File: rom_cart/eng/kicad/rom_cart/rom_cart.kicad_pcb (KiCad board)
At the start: 2 copper layers, 128.3 x 99.1 mm, 12 parts, among them J1 CONN_A2K6_CART_CARD, J2 CONN_512K_CART_CARD, SW1 SW_DIP_x04, SW2 SW_DIP_x04, U1 SST39SF040-70-4C-NHE, U2 74AHCT1G04

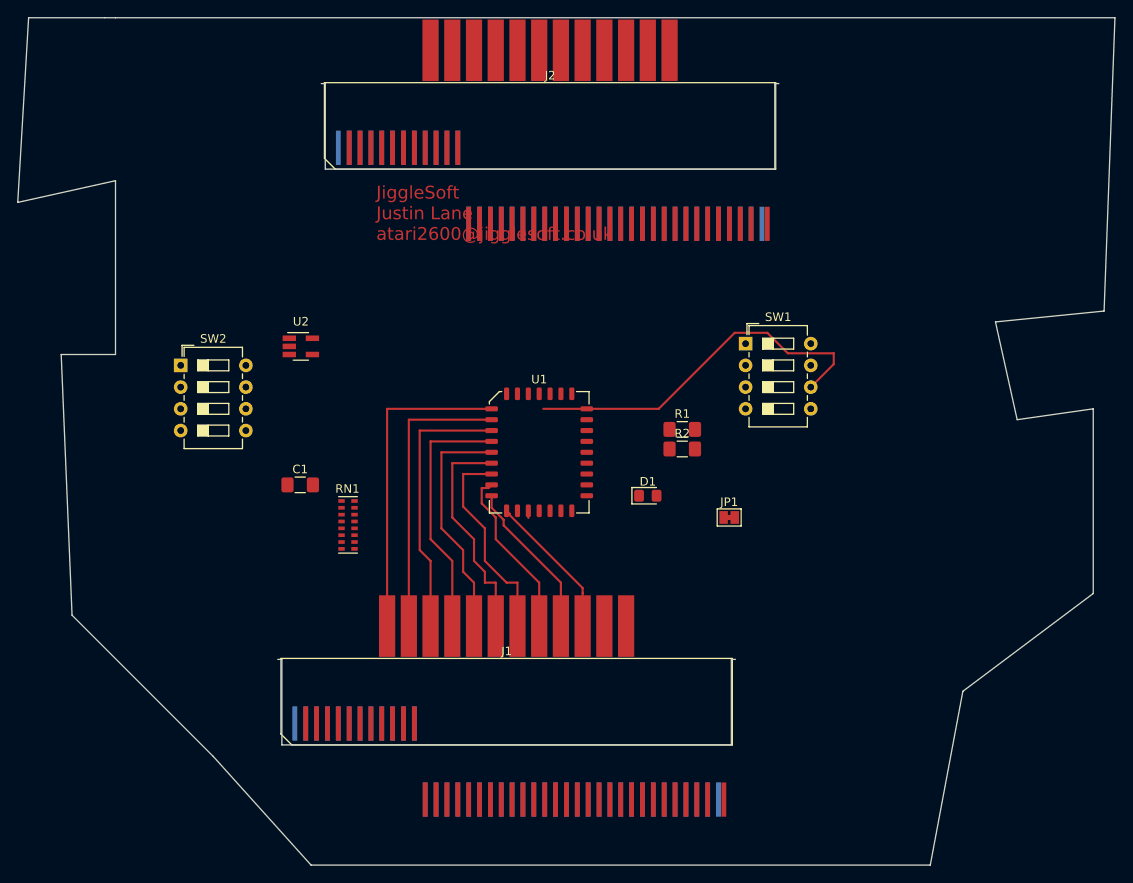
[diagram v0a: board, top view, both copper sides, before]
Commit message: Atari 2600 Budget Flash ROM Cartridge PCB layout Work-In-Progress.
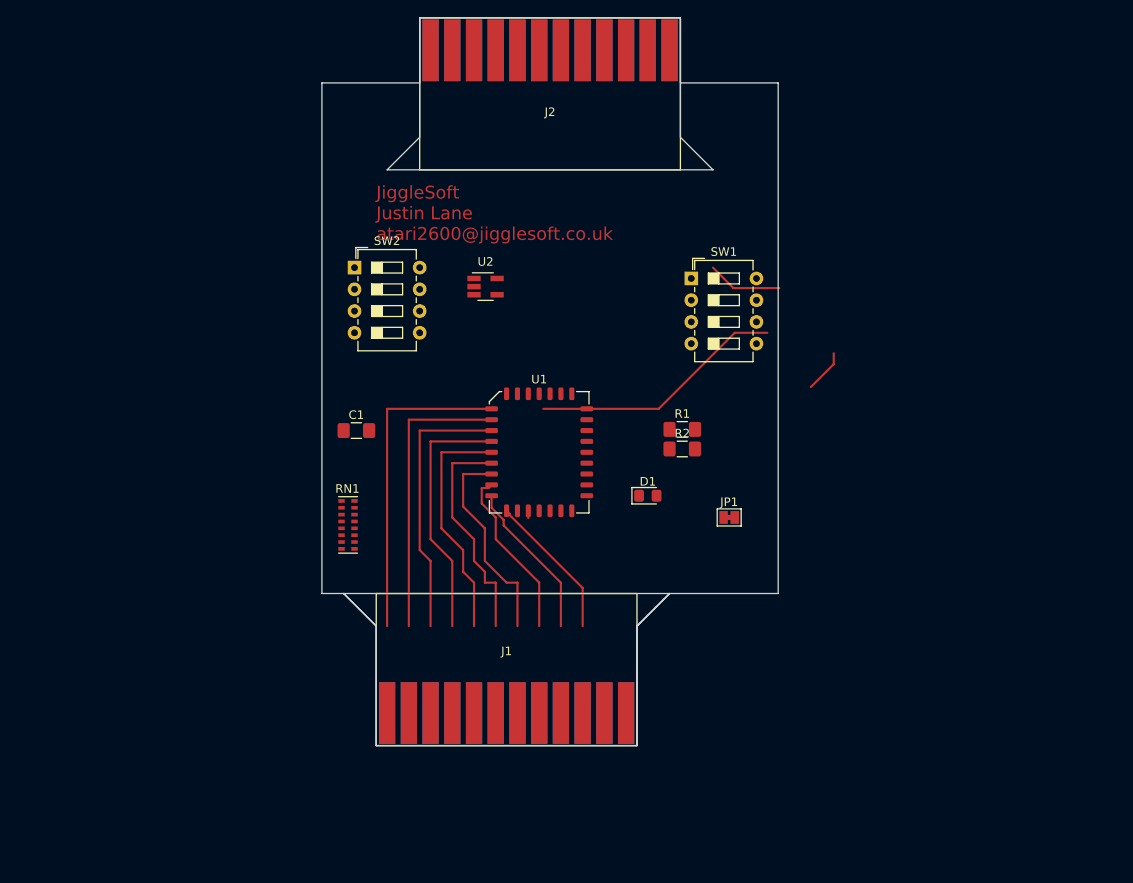
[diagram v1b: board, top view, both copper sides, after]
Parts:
- moved SW2 23.3 mm to (125.7, 66.0)
- moved U2 22.7 mm to (141.1, 68.3)
- moved SW1 9.92 mm to (165.1, 67.3)
- moved C1 9.14 mm to (125.9, 85.1)
- moved J2 7.62 mm to (148.6, 41.9), turned to 180 degrees
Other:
- board size 128.3 x 99.1 mm -> 53.3 x 85.1 mm

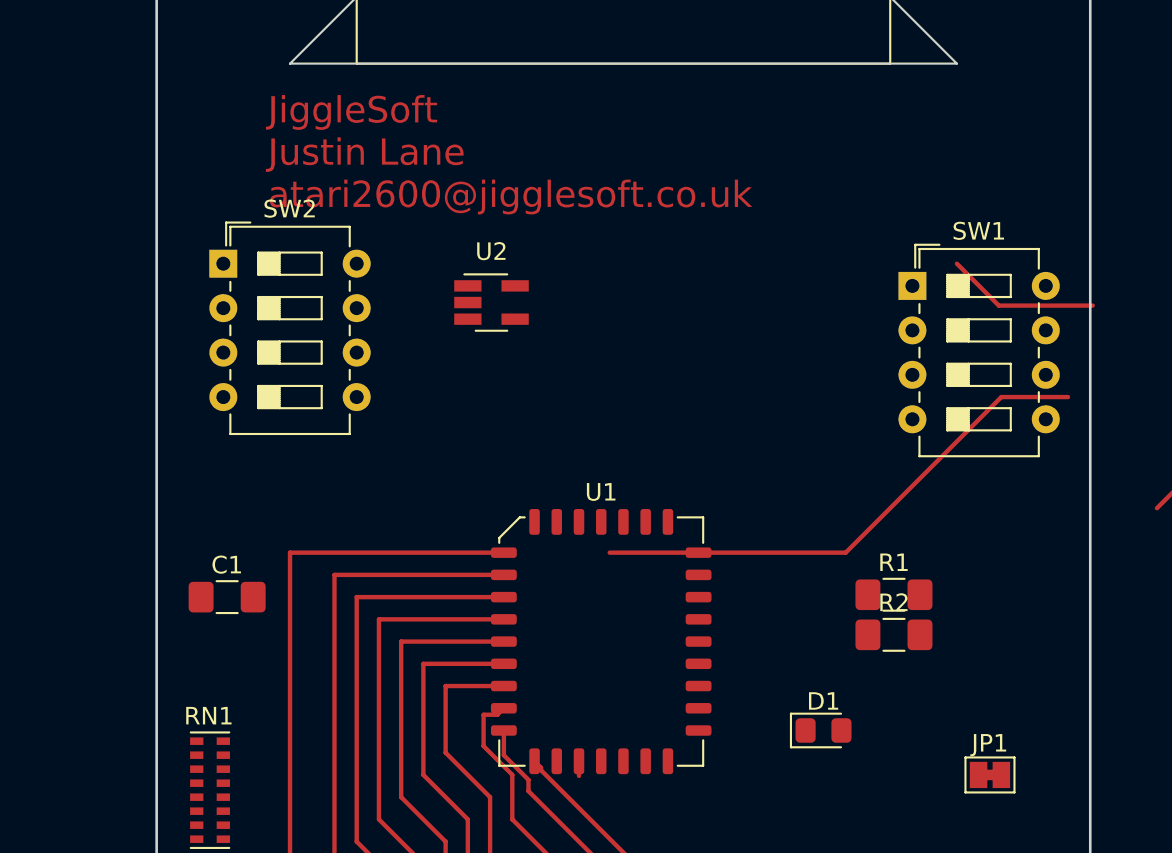
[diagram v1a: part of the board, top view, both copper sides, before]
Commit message: Updated licence for cart_programmer schematic. Updated licence for rom_ram_pld_cart schematic. Updated component references from both of those schematics. Latest cartridge programmer serial protocol checked in for backup (WIP).
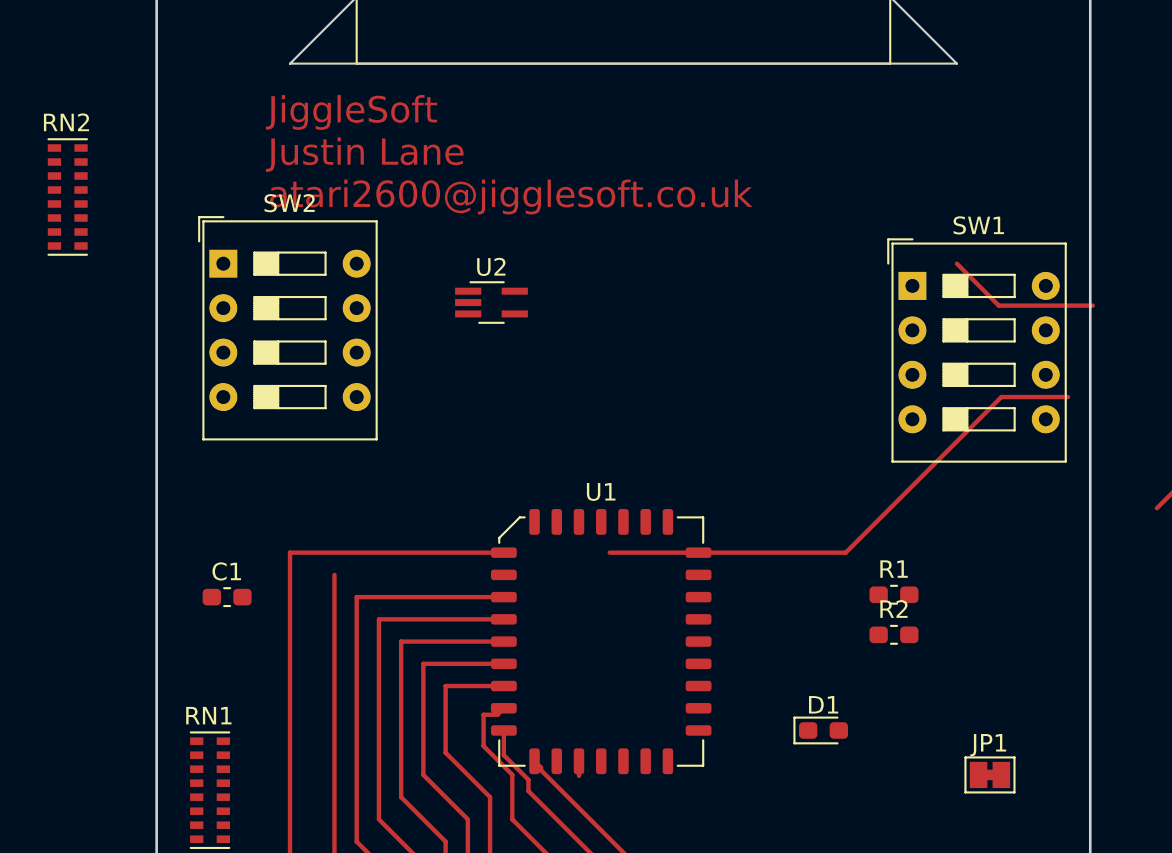
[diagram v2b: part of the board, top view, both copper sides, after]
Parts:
- added RN2: R470 X 8, Resistor_SMD:R_Cat16-8, F.Cu at (116.8, 62.2)
- C1: footprint Capacitor_SMD:C_1206_3216Metric_Pad1.42x1.75mm_HandSolder -> Capacitor_SMD:C_0603_1608Metric_Pad1.05x0.95mm_HandSolder
- D1: footprint LED_SMD:LED_0805_2012Metric_Pad1.15x1.40mm_HandSolder -> LED_SMD:LED_0603_1608Metric_Pad1.05x0.95mm_HandSolder
- J1, J2: footprint JiggleSoft_Conn_Atari:Atari_2600_Cartridge_2x12_PCB_Edge -> Conn_Atari_JiggleSoft:Atari_2600_Cartridge_2x12_PCB_Edge
- R1, R2: footprint Resistor_SMD:R_1206_3216Metric_Pad1.42x1.75mm_HandSolder -> Resistor_SMD:R_0603_1608Metric_Pad1.05x0.95mm_HandSolder
- RN1: value R_Pack08 -> 10K X 8
- SW1, SW2: footprint Button_Switch_THT:SW_DIP_SPSTx04_Slide_6.7x11.72mm_W7.62mm_P2.54mm_LowProfile -> Button_Switch_THT:SW_DIP_SPSTx04_Slide_9.78x12.34mm_W7.62mm_P2.54mm
- U2: value 74AHCT1G04 -> 74HCT1G04; footprint Package_TO_SOT_SMD:SOT-23-5_HandSoldering -> Package_TO_SOT_SMD:SOT-353_SC-70-5_Handsoldering
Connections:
- net /CS renamed /CE
- net Net-(U1-Pad22) renamed /~CE
- J2 pad 14: Net-(J2-Pad14) -> (no net)
- J2 pad 18: Net-(J2-Pad18) -> (no net)
- J2 pad 19: Net-(J2-Pad18) -> GND
- J2 pad 23: Net-(J2-Pad23) -> (no net)
- RN1 pad 1: Net-(RN1-Pad1) -> GND
- RN1 pad 2: Net-(RN1-Pad1) -> GND
- RN1 pad 3: Net-(RN1-Pad1) -> GND
- RN1 pad 4: Net-(RN1-Pad1) -> GND
- RN1 pad 5: Net-(RN1-Pad1) -> GND
- RN1 pad 6: Net-(RN1-Pad1) -> GND
- RN1 pad 7: Net-(RN1-Pad1) -> GND
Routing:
- net /A6: track 33.8 -> 24.1 mm
